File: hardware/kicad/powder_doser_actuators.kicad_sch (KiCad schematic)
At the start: 11 parts, among them J1 Pi Zero 2 W on Perma-Proto Bo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, J2 5 V PSU input (Adafruit #373), J3 12 V PSU input, M1 ERM coin motor (#1201) or LRA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, M2 NEMA 11 bipolar stepper, U1 Adafruit DRV2605L (#2305), U2 Adafruit DRV8871 (#3190), U3 Pololu DRV8825 carrier (#2133)

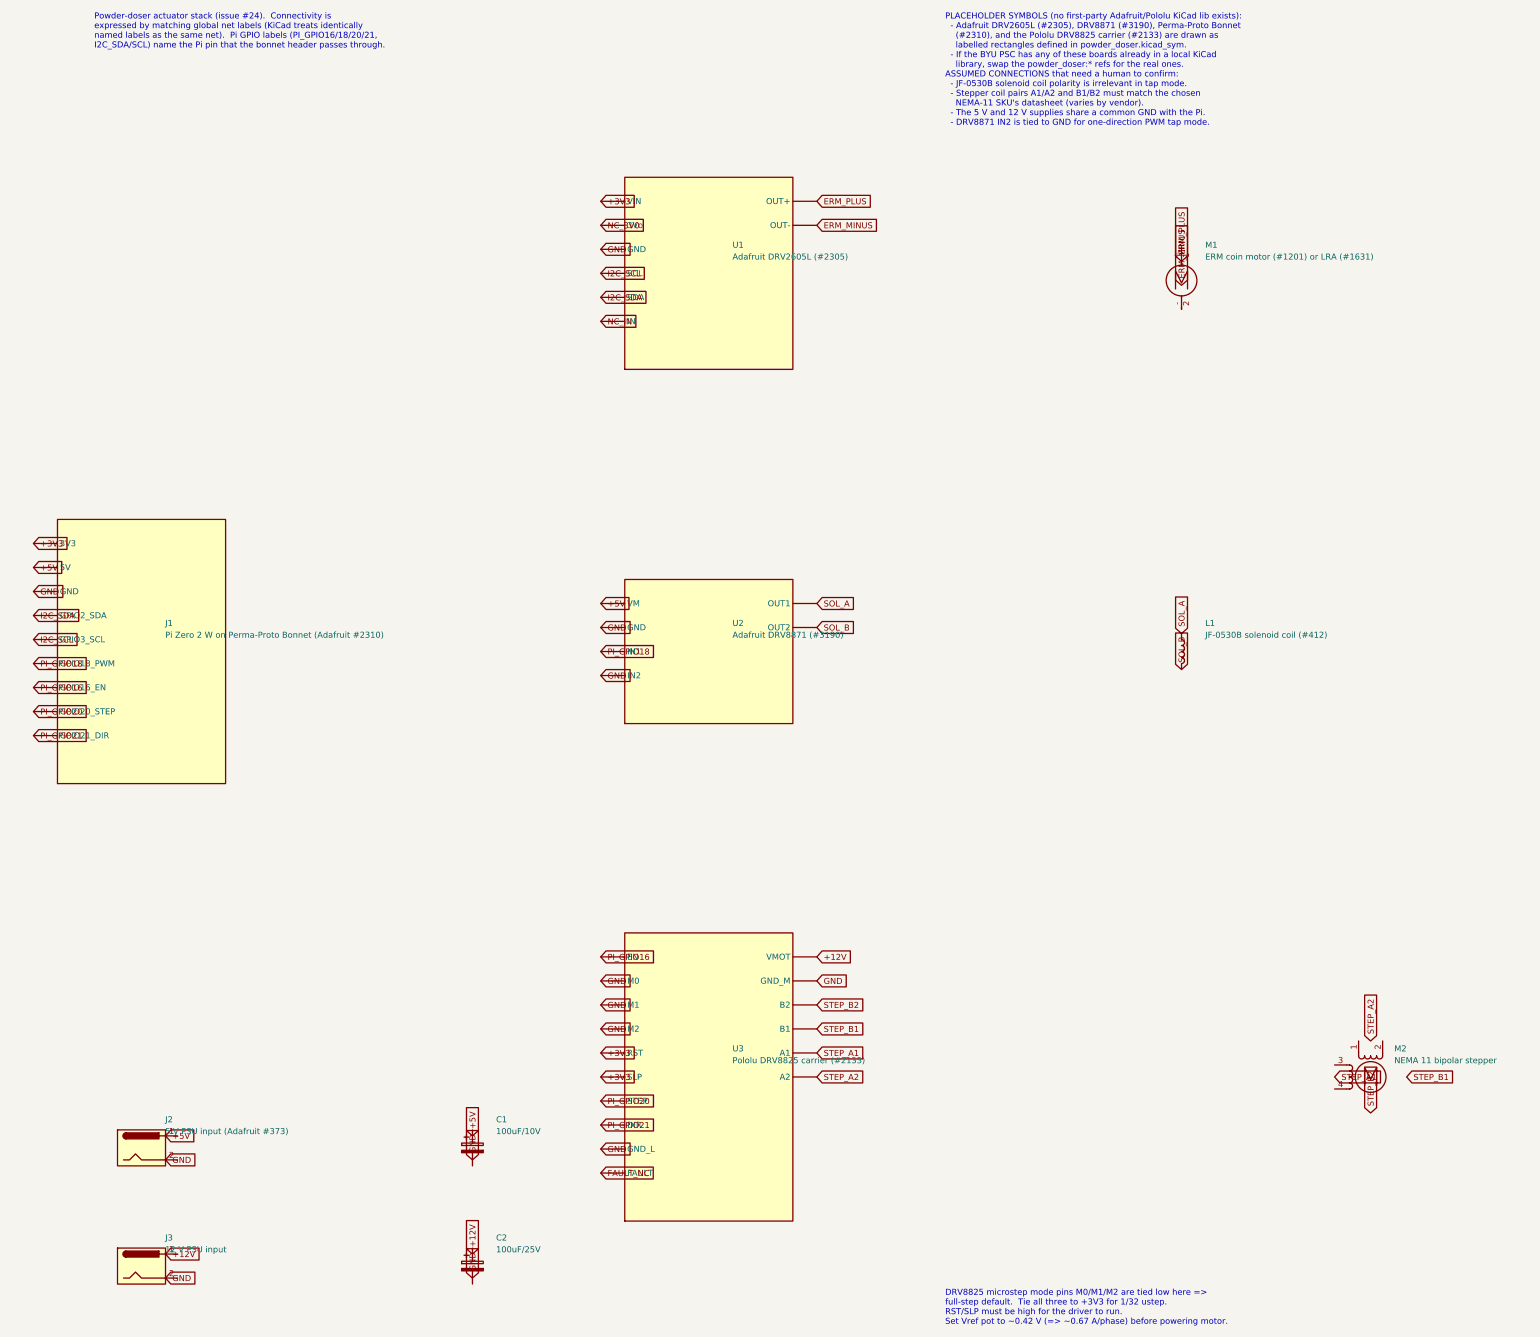
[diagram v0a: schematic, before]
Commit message: Improve KiCad schematic layout: pull global labels off symbol bodies via wire stubs
Agent-Logs-Url: https://github.com/vertical-cloud-lab/powder-doser/sessions/e898731e-d2b1-4dbb-bfa7-52bd318030df

Co-authored-by: swcharles <185848910+swcharles@users.noreply.github.com>
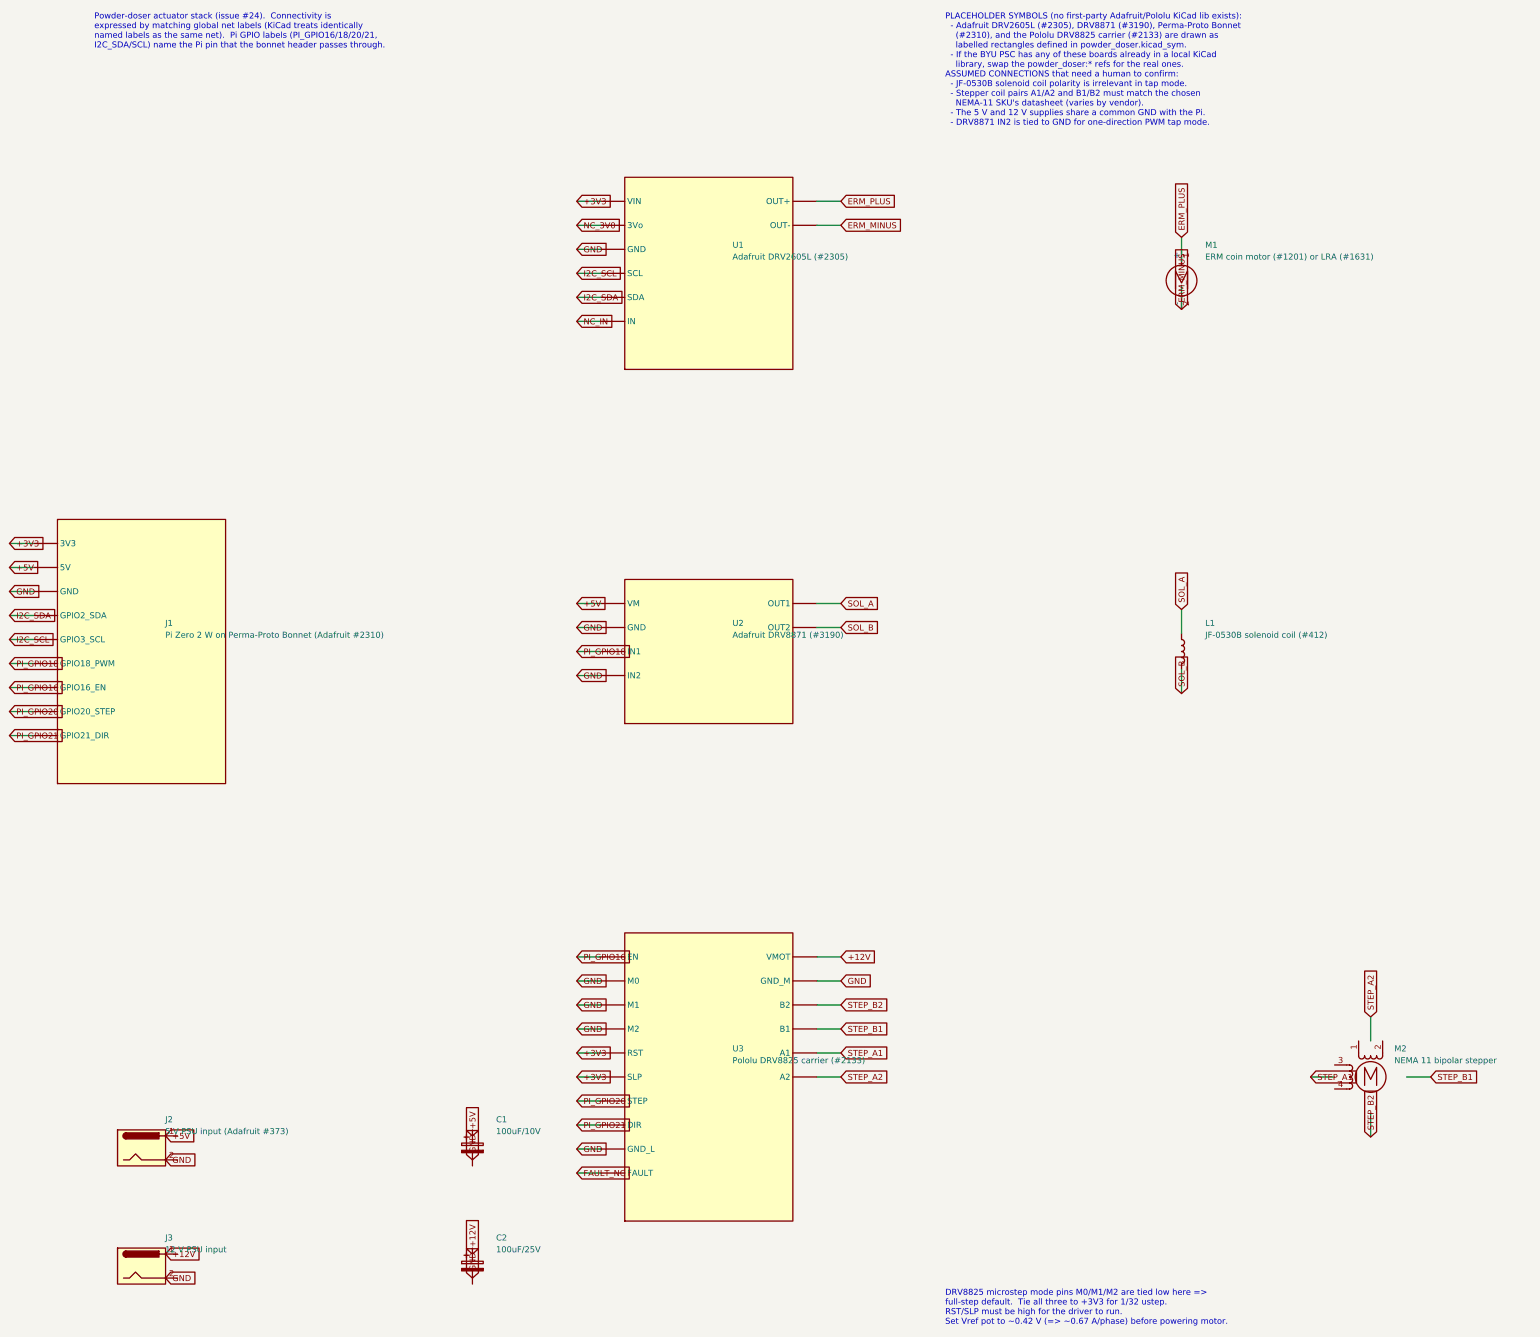
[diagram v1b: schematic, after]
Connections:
- net ERM_MINUS: now also M1.2 (-)
